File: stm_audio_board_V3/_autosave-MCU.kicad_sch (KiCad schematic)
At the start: 41 parts, among them J10 USB_A, SW1 SW_SPST, U1 IS42S16100H-7TL, U16 USBLC6-2P6, U17 W25Q128JVS, U19 FE1.1s, U7 STM32H723ZGTx, Y2 X1E0000210132, Y3 Crystal_GND24

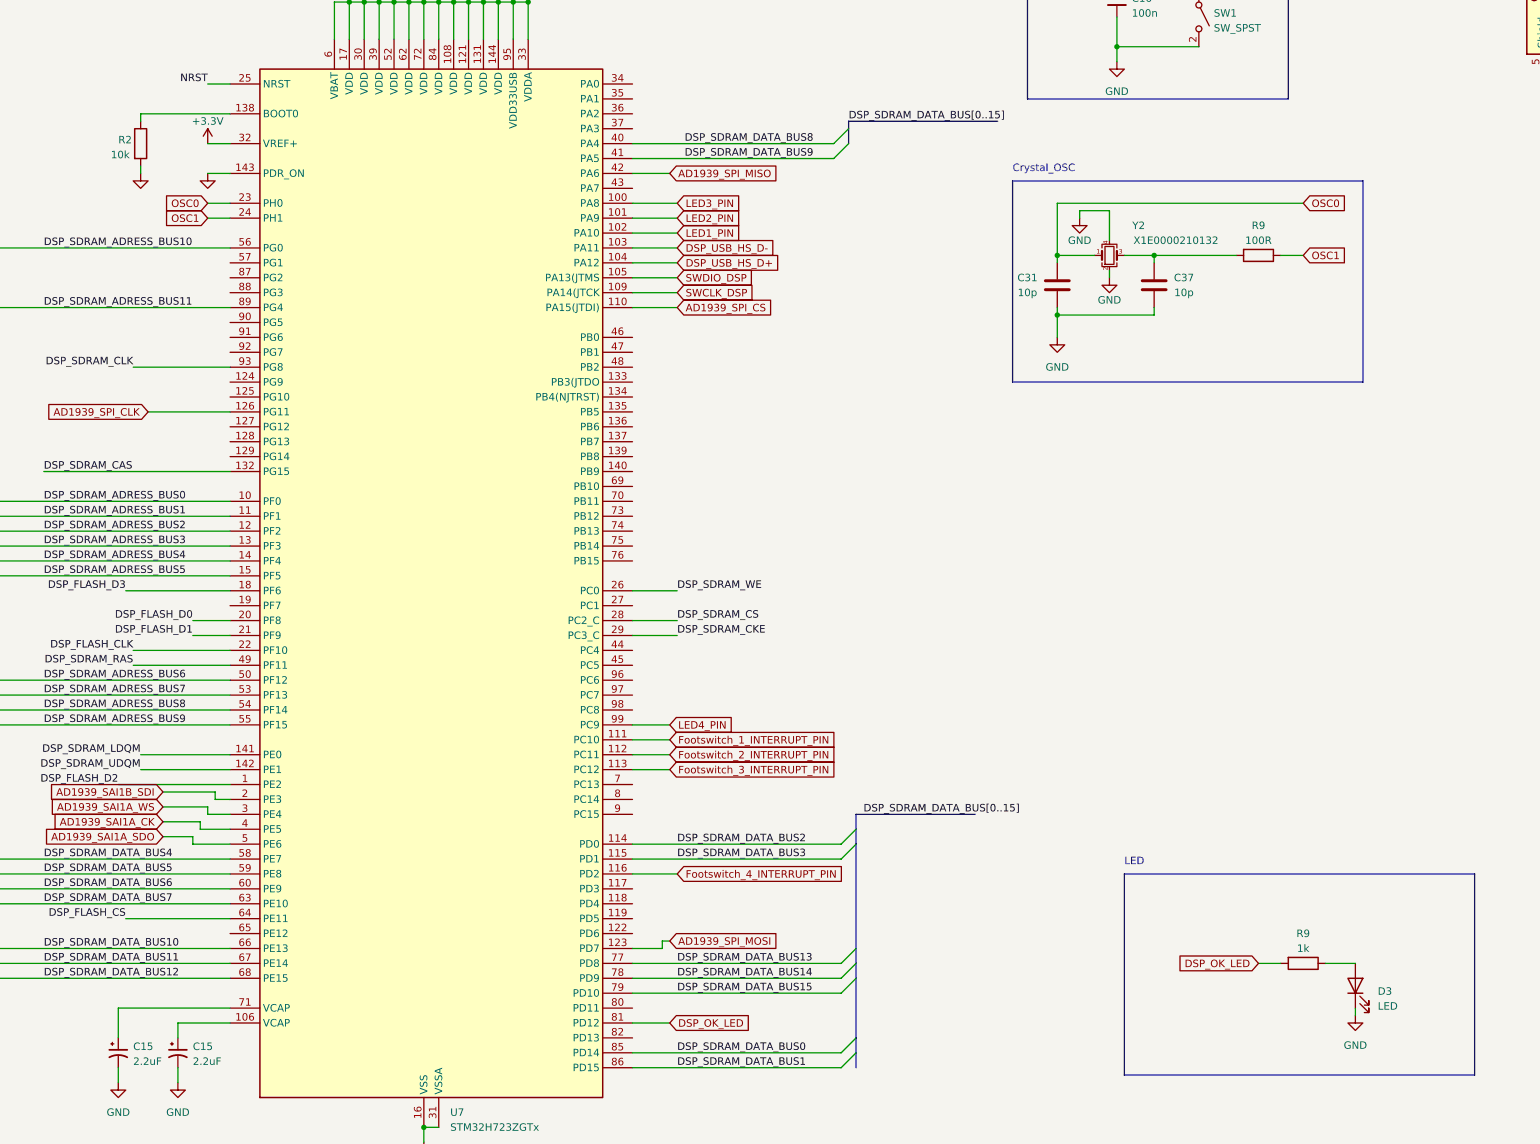
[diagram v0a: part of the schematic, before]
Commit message: added external pot, added feedback leds, added I2C between MCUs
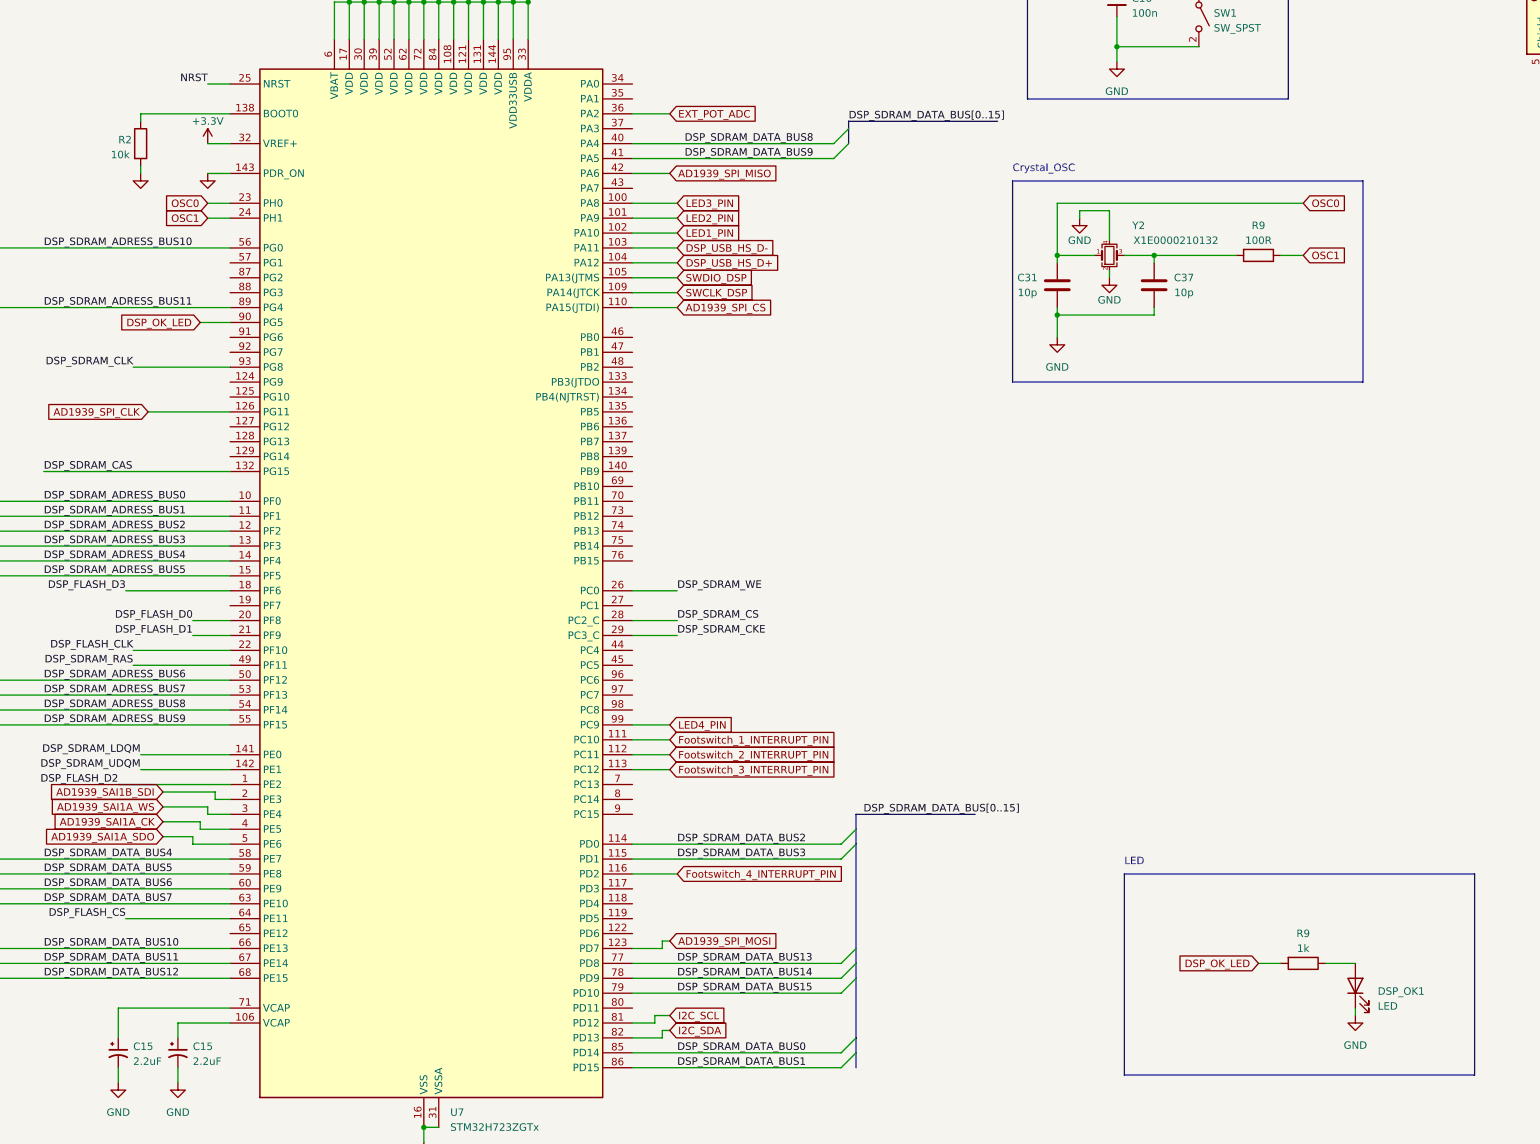
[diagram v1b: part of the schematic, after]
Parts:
- renumbered D3 to DSP_OK1
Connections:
- net DSP_OK_LED: now also U7.90 (PG5); no longer U7.81 (PD12)
- net EXT_POT_ADC: now reaches U7.36 (PA2)
- net I2C_SDA: now reaches U7.82 (PD13)
- new net I2C_SCL: U7.81 (PD12)
